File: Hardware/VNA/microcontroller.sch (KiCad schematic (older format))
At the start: 64 parts, among them SW1 SW_Push, SW2 SW_Push, SW3 SW_Push, U16 STM32F373RCTx, U17 AT25SF081-SSHD-X, Y1 8MHz

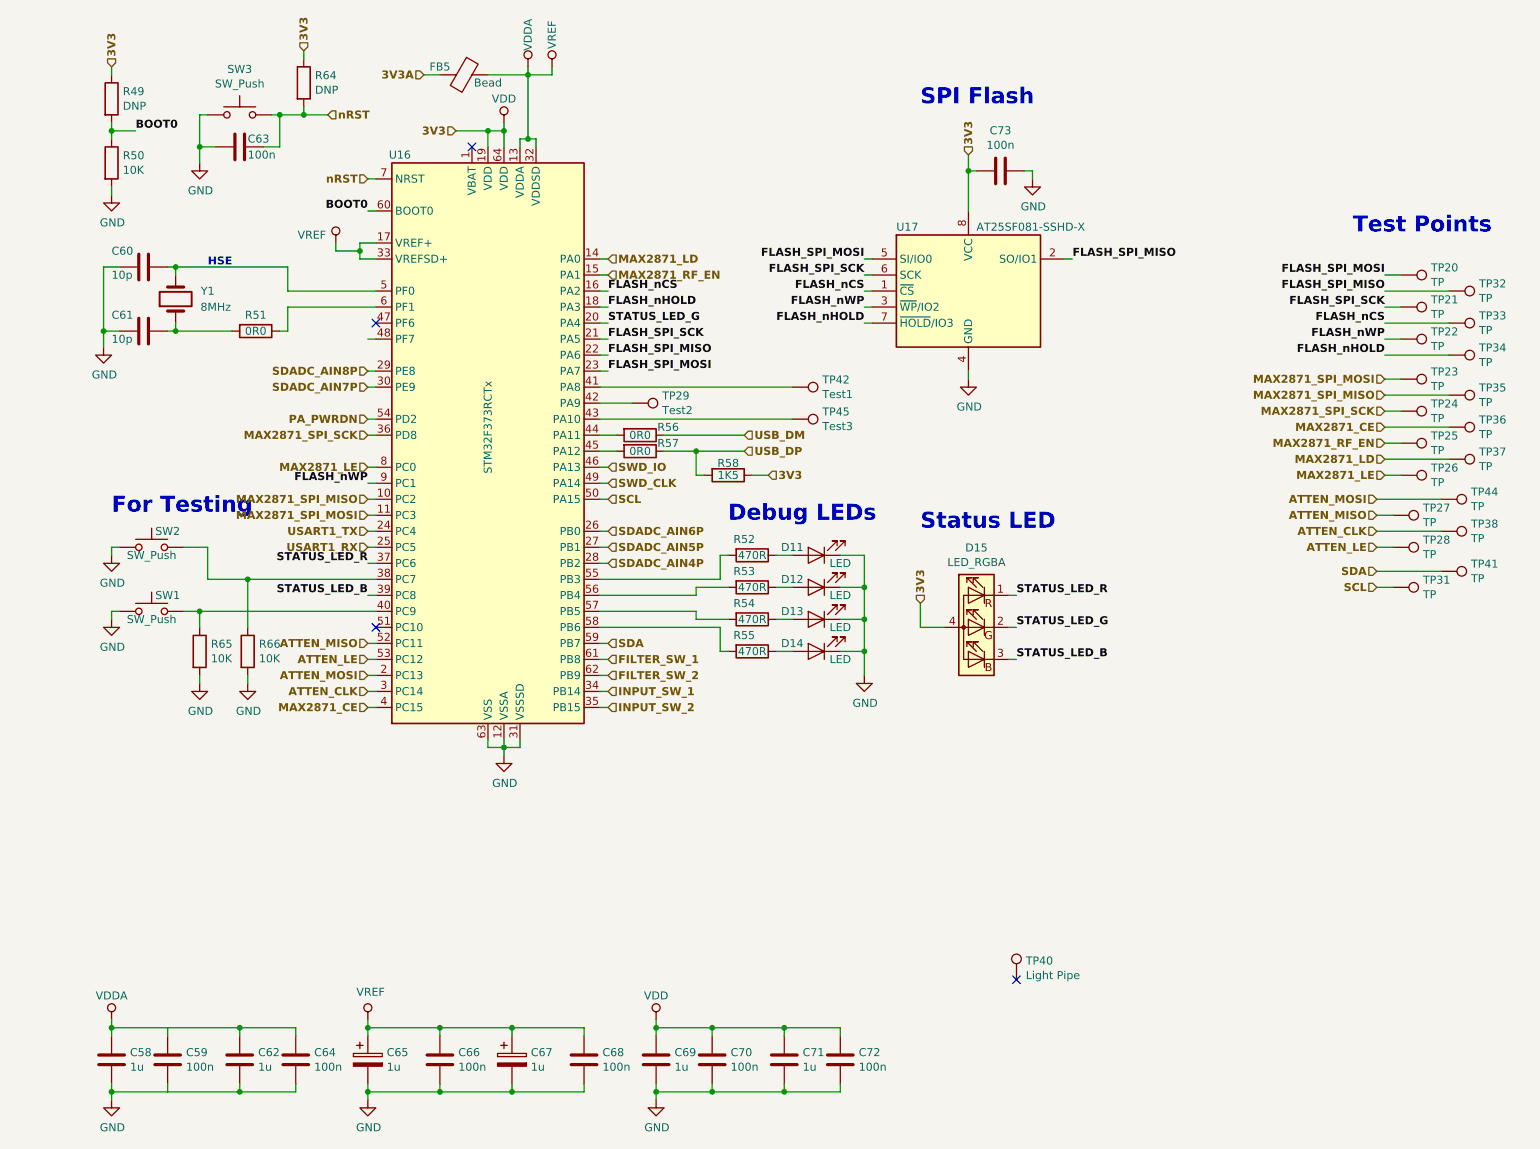
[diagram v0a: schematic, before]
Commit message: fix KiCad 5.1.0 bold after plot issue on schematics
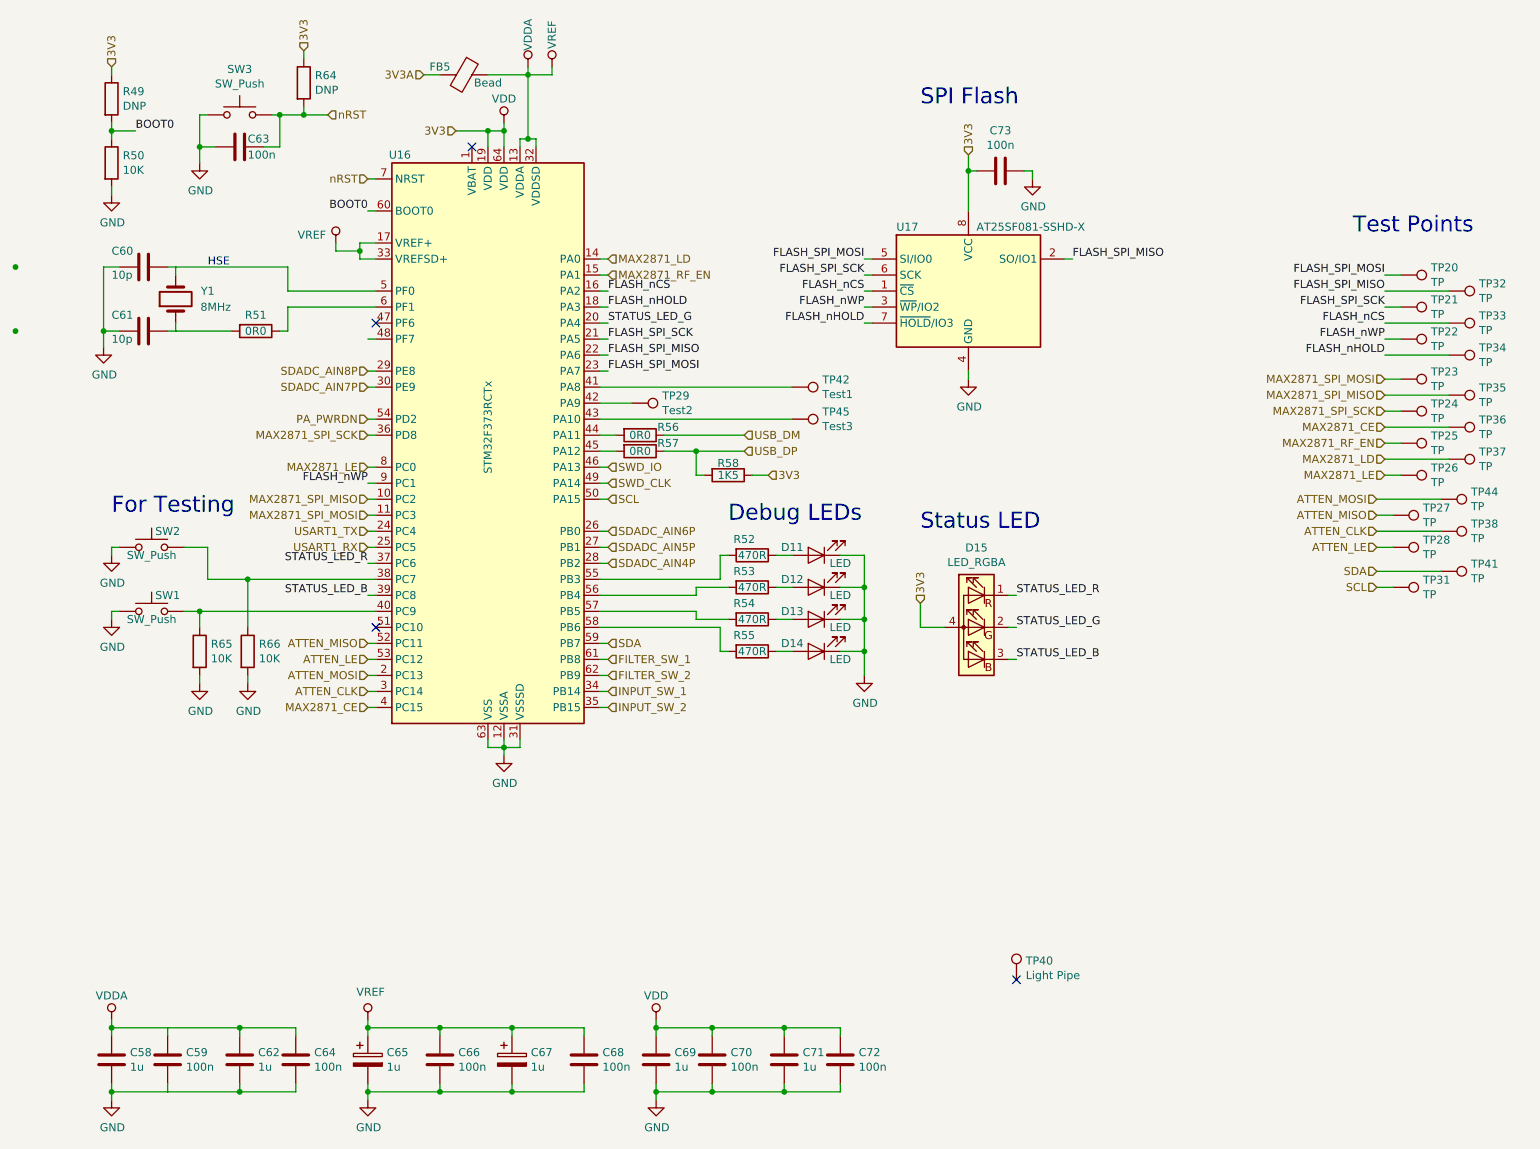
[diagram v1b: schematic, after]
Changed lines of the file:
@@
 Wire Wire Line
 	650  1450 650  1500
-Text HLabel 650  1100 1    50   Input ~ 10
+Text HLabel 650  1100 1    50   Input ~ 0
 3V3
 Wire Wire Line
@@
 Wire Wire Line
 	650  1500 650  1550
-Text Label 800  1500 0    50   ~ 10
+Text Label 800  1500 0    50   ~ 0
 BOOT0
 Wire Wire Line
@@
 	1    0    0    -1
 $EndComp
-Text HLabel 2000 1400 2    50   Input ~ 10
+Text HLabel 2000 1400 2    50   Input ~ 0
 nRST
-Text HLabel 6000 1650 1    50   Input ~ 10
+Text HLabel 6000 1650 1    50   Input ~ 0
 3V3
 $Comp
@@
 	1    0    0    -1
 $EndComp
-Text Label 6650 2300 0    50   ~ 10
+Text Label 6650 2300 0    50   ~ 0
 FLASH_SPI_MISO
-Text Label 5350 2300 2    50   ~ 10
+Text Label 5350 2300 2    50   ~ 0
 FLASH_SPI_MOSI
-Text Label 5350 2400 2    50   ~ 10
+Text Label 5350 2400 2    50   ~ 0
 FLASH_SPI_SCK
-Text Label 5350 2500 2    50   ~ 10
+Text Label 5350 2500 2    50   ~ 0
 FLASH_nCS
-Text Label 5350 2600 2    50   ~ 10
+Text Label 5350 2600 2    50   ~ 0
 FLASH_nWP
-Text Label 5350 2700 2    50   ~ 10
+Text Label 5350 2700 2    50   ~ 0
 FLASH_nHOLD
-Text Notes 5700 1350 0    100  ~ 20
+Text Notes 5700 1350 0    100  ~ 0
 SPI Flash
 Wire Wire Line
@@
 Wire Wire Line
 	6250 4800 6300 4800
-Text HLabel 5700 4450 1    50   Input ~ 10
+Text HLabel 5700 4450 1    50   Input ~ 0
 3V3
-Text Label 6300 4400 0    50   ~ 10
+Text Label 6300 4400 0    50   ~ 0
 STATUS_LED_R
-Text Label 6300 4600 0    50   ~ 10
+Text Label 6300 4600 0    50   ~ 0
 STATUS_LED_G
-Text Label 6300 4800 0    50   ~ 10
+Text Label 6300 4800 0    50   ~ 0
 STATUS_LED_B
-Text Notes 5700 4000 0    100  ~ 20
+Text Notes 5700 4000 0    100  ~ 0
 Status LED
 Wire Wire Line
@@
 Wire Wire Line
 	3750 2700 3700 2700
-Text Label 2250 4400 2    50   ~ 10
+Text Label 2250 4400 2    50   ~ 0
 STATUS_LED_B
-Text Label 3750 2700 0    50   ~ 10
+Text Label 3750 2700 0    50   ~ 0
 STATUS_LED_G
-Text Label 2250 4200 2    50   ~ 10
+Text Label 2250 4200 2    50   ~ 0
 STATUS_LED_R
-Text Label 3750 2600 0    50   ~ 10
+Text Label 3750 2600 0    50   ~ 0
 FLASH_nHOLD
 Wire Wire Line
 	2300 5100 2250 5100
-Text Label 2250 3700 2    50   ~ 10
+Text Label 2250 3700 2    50   ~ 0
 FLASH_nWP
 Wire Wire Line
 	2300 3600 2250 3600
-Text Label 3750 2500 0    50   ~ 10
+Text Label 3750 2500 0    50   ~ 0
 FLASH_nCS
 Wire Wire Line
 	2300 3700 2250 3700
-Text Label 3750 2800 0    50   ~ 10
+Text Label 3750 2800 0    50   ~ 0
 FLASH_SPI_SCK
-Text HLabel 3750 4700 2    50   Input ~ 10
+Text HLabel 3750 4700 2    50   Input ~ 0
 SDA
 Wire Wire Line
@@
 Wire Wire Line
 	3750 3800 3700 3800
-Text HLabel 2250 1800 0    50   Input ~ 10
+Text HLabel 2250 1800 0    50   Input ~ 0
 nRST
-Text HLabel 4600 3500 2    50   Input ~ 10
+Text HLabel 4600 3500 2    50   Input ~ 0
 USB_DP
-Text HLabel 4600 3400 2    50   Input ~ 10
+Text HLabel 4600 3400 2    50   Input ~ 0
 USB_DM
 Wire Wire Line
 	2300 3400 2250 3400
-Text HLabel 2250 4100 0    50   Input ~ 10
+Text HLabel 2250 4100 0    50   Input ~ 0
 USART1_RX
-Text HLabel 2250 4000 0    50   Input ~ 10
+Text HLabel 2250 4000 0    50   Input ~ 0
 USART1_TX
 Wire Wire Line
@@
 Wire Wire Line
 	2300 4000 2250 4000
-Text HLabel 2250 3900 0    50   Input ~ 10
+Text HLabel 2250 3900 0    50   Input ~ 0
 MAX2871_SPI_MOSI
-Text HLabel 2250 3800 0    50   Input ~ 10
+Text HLabel 2250 3800 0    50   Input ~ 0
 MAX2871_SPI_MISO
-Text HLabel 2250 3400 0    50   Input ~ 10
+Text HLabel 2250 3400 0    50   Input ~ 0
 MAX2871_SPI_SCK
 Wire Wire Line
@@
 Wire Wire Line
 	3700 2800 3750 2800
-Text Label 3750 3000 0    50   ~ 10
+Text Label 3750 3000 0    50   ~ 0
 FLASH_SPI_MOSI
-Text Label 3750 2900 0    50   ~ 10
+Text Label 3750 2900 0    50   ~ 0
 FLASH_SPI_MISO
 Wire Wire Line
@@
 	0    1    1    0
 $EndComp
-Text HLabel 2800 1500 0    50   Input ~ 10
+Text HLabel 2800 1500 0    50   Input ~ 0
 3V3
 Connection ~ 3100 1500
@@
 Wire Wire Line
 	2300 2300 2200 2300
-Text HLabel 2600 1150 0    50   Input ~ 10
+Text HLabel 2600 1150 0    50   Input ~ 0
 3V3A
 Wire Wire Line
@@
 	1    0    0    -1
 $EndComp
-Text Label 2250 2000 2    50   ~ 10
+Text Label 2250 2000 2    50   ~ 0
 BOOT0
 Wire Wire Line
@@
 Wire Wire Line
 	1700 2750 1750 2750
-Connection ~ 1050 2750
+Connection ~ 050 2750
 Wire Wire Line
 	1400 2750 1050 2750
@@
 	0    1    1    0
 $EndComp
-Text Notes 1250 2350 0    50   ~ 10
+Text Notes 1250 2350 0    50   ~ 0
 HSE
-Connection ~ 1050 2350
+Connection ~ 050 2350
 Wire Wire Line
 	1750 2350 1050 2350
@@
 Wire Wire Line
 	3000 5300 3000 5350
-Text HLabel 3750 4000 2    50   Input ~ 10
+Text HLabel 3750 4000 2    50   Input ~ 0
 SDADC_AIN6P
 Wire Wire Line
@@
 Wire Wire Line
 	2250 3100 2300 3100
-Text HLabel 3750 4100 2    50   Input ~ 10
+Text HLabel 3750 4100 2    50   Input ~ 0
 SDADC_AIN5P
-Text HLabel 3750 4200 2    50   Input ~ 10
+Text HLabel 3750 4200 2    50   Input ~ 0
 SDADC_AIN4P
-Text HLabel 2250 3000 0    50   Input ~ 10
+Text HLabel 2250 3000 0    50   Input ~ 0
 SDADC_AIN8P
-Text HLabel 2250 3100 0    50   Input ~ 10
+Text HLabel 2250 3100 0    50   Input ~ 0
 SDADC_AIN7P
-Text HLabel 2250 5100 0    50   Input ~ 10
+Text HLabel 2250 5100 0    50   Input ~ 0
 MAX2871_CE
 Wire Wire Line
@@
 Wire Wire Line
 	3700 2300 3750 2300
-Text HLabel 3750 2400 2    50   Input ~ 10
+Text HLabel 3750 2400 2    50   Input ~ 0
 MAX2871_RF_EN
-Text HLabel 3750 2300 2    50   Input ~ 10
+Text HLabel 3750 2300 2    50   Input ~ 0
 MAX2871_LD
-Text HLabel 2250 3600 0    50   Input ~ 10
+Text HLabel 2250 3600 0    50   Input ~ 0
 MAX2871_LE
 Wire Wire Line
@@
 Wire Wire Line
 	3700 5100 3750 5100
-Text HLabel 3750 5000 2    50   Input ~ 10
+Text HLabel 3750 5000 2    50   Input ~ 0
 INPUT_SW_1
-Text HLabel 3750 5100 2    50   Input ~ 10
+Text HLabel 3750 5100 2    50   Input ~ 0
 INPUT_SW_2
-Text HLabel 2250 4900 0    50   Input ~ 10
+Text HLabel 2250 4900 0    50   Input ~ 0
 ATTEN_MOSI
 Wire Wire Line
 	2300 3300 2250 3300
-Text HLabel 2250 5000 0    50   Input ~ 10
+Text HLabel 2250 5000 0    50   Input ~ 0
 ATTEN_CLK
-Text HLabel 2250 4800 0    50   Input ~ 10
+Text HLabel 2250 4800 0    50   Input ~ 0
 ATTEN_LE
-Text HLabel 2250 3300 0    50   Input ~ 10
+Text HLabel 2250 3300 0    50   Input ~ 0
 PA_PWRDN
-Text HLabel 3750 4800 2    50   Input ~ 10
+Text HLabel 3750 4800 2    50   Input ~ 0
 FILTER_SW_1
-Text HLabel 3750 4900 2    50   Input ~ 10
+Text HLabel 3750 4900 2    50   Input ~ 0
 FILTER_SW_2
 Wire Wire Line
@@
 	0    1    1    0
 $EndComp
-Text Notes 4500 3950 0    100  ~ 20
+Text Notes 4500 3950 0    100  ~ 0
 Debug LEDs
 $Comp
@@
 Wire Wire Line
 	1250 4300 1500 4300
-Text Notes 650  3900 0    100  ~ 20
+Text Notes 650  3900 0    100  ~ 0
 For Testing
 Wire Wire Line
@@
 Wire Wire Line
 	3700 3700 3750 3700
-Text HLabel 3750 3600 2    50   Input ~ 10
+Text HLabel 3750 3600 2    50   Input ~ 0
 SWD_IO
-Text HLabel 3750 3700 2    50   Input ~ 10
+Text HLabel 3750 3700 2    50   Input ~ 0
 SWD_CLK
-Text HLabel 3750 3800 2    50   Input ~ 10
+Text HLabel 3750 3800 2    50   Input ~ 0
 SCL
 $Comp
@@
 	0    1    1    0
 $EndComp
-Text HLabel 4750 3650 2    50   Input ~ 10
+Text HLabel 4750 3650 2    50   Input ~ 0
 3V3
 $Comp
@@
 Wire Wire Line
 	4650 3650 4750 3650
-Text Label 8600 2400 2    50   ~ 10
+Text Label 8600 2400 2    50   ~ 0
 FLASH_SPI_MOSI
-Text Label 8600 2600 2    50   ~ 10
+Text Label 8600 2600 2    50   ~ 0
 FLASH_SPI_SCK
-Text Label 8600 2700 2    50   ~ 10
+Text Label 8600 2700 2    50   ~ 0
 FLASH_nCS
-Text Label 8600 2800 2    50   ~ 10
+Text Label 8600 2800 2    50   ~ 0
 FLASH_nWP
-Text Label 8600 2900 2    50   ~ 10
+Text Label 8600 2900 2    50   ~ 0
 FLASH_nHOLD
-Text Label 8600 2500 2    50   ~ 10
+Text Label 8600 2500 2    50   ~ 0
 FLASH_SPI_MISO
-Text Notes 8400 2150 0    100  ~ 20
+Text Notes 8400 2150 0    100  ~ 0
 Test Points
-Text HLabel 8600 3050 0    50   Input ~ 10
+Text HLabel 8600 3050 0    50   Input ~ 0
 MAX2871_SPI_MOSI
-Text HLabel 8600 3150 0    50   Input ~ 10
+Text HLabel 8600 3150 0    50   Input ~ 0
 MAX2871_SPI_MISO
-Text HLabel 8600 3250 0    50   Input ~ 10
+Text HLabel 8600 3250 0    50   Input ~ 0
 MAX2871_SPI_SCK
-Text HLabel 8600 3350 0    50   Input ~ 10
+Text HLabel 8600 3350 0    50   Input ~ 0
 MAX2871_CE
-Text HLabel 8600 3450 0    50   Input ~ 10
+Text HLabel 8600 3450 0    50   Input ~ 0
 MAX2871_RF_EN
-Text HLabel 8600 3550 0    50   Input ~ 10
+Text HLabel 8600 3550 0    50   Input ~ 0
 MAX2871_LD
-Text HLabel 8600 3650 0    50   Input ~ 10
+Text HLabel 8600 3650 0    50   Input ~ 0
 MAX2871_LE
-Text HLabel 8550 4000 0    50   Input ~ 10
+Text HLabel 8550 4000 0    50   Input ~ 0
 ATTEN_CLK
-Text HLabel 8550 4100 0    50   Input ~ 10
+Text HLabel 8550 4100 0    50   Input ~ 0
 ATTEN_LE
-Text HLabel 8550 4250 0    50   Input ~ 10
+Text HLabel 8550 4250 0    50   Input ~ 0
 SDA
-Text HLabel 8550 4350 0    50   Input ~ 10
+Text HLabel 8550 4350 0    50   Input ~ 0
 SCL
 $Comp
@@
 Wire Wire Line
 	8650 4350 8550 4350
-Text HLabel 2250 4700 0    50   Input ~ 10
+Text HLabel 2250 4700 0    50   Input ~ 0
 ATTEN_MISO
 Wire Wire Line
@@
 Wire Wire Line
 	1750 2500 2300 2500
-Text HLabel 8550 3900 0    50   Input ~ 10
+Text HLabel 8550 3900 0    50   Input ~ 0
 ATTEN_MISO
-Text HLabel 8550 3800 0    50   Input ~ 10
+Text HLabel 8550 3800 0    50   Input ~ 0
 ATTEN_MOSI
 $Comp
@@
 Wire Wire Line
 	1850 1400 2000 1400
-Text HLabel 1850 1000 1    50   Input ~ 10
+Text HLabel 1850 1000 1    50   Input ~ 0
 3V3
 Wire Wire Line
